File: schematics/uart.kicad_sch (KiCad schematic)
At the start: 5 parts, among them U10 W65C51NxP, Y2 1.8432MHz

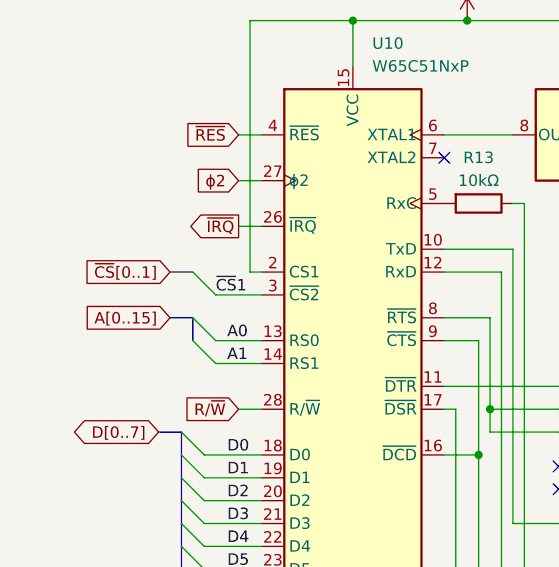
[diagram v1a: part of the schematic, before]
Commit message: Address decoder pld file and no-VIA keyboard schematic and pld file.
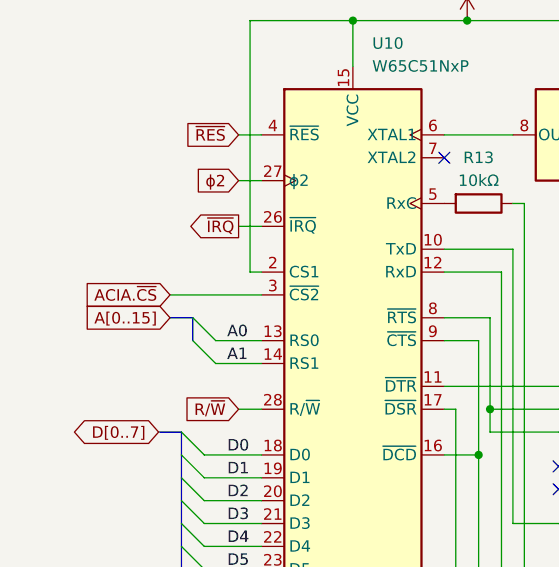
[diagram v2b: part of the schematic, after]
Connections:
- net ~{CS}1 renamed ACIA.~{CS}

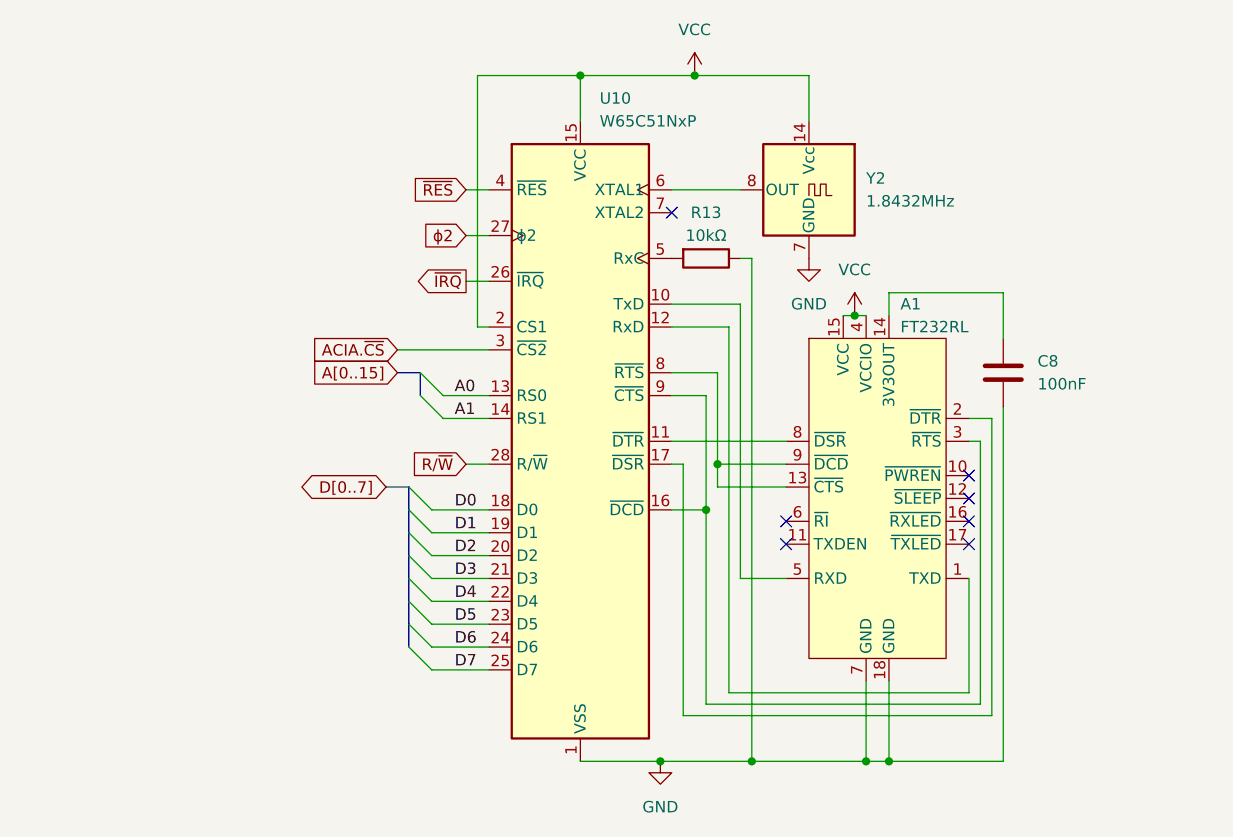
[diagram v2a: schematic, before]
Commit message: PLD files and schematics for address decoder, device selector, keyboard controller, lcd controller, banked memory, and bootloader.
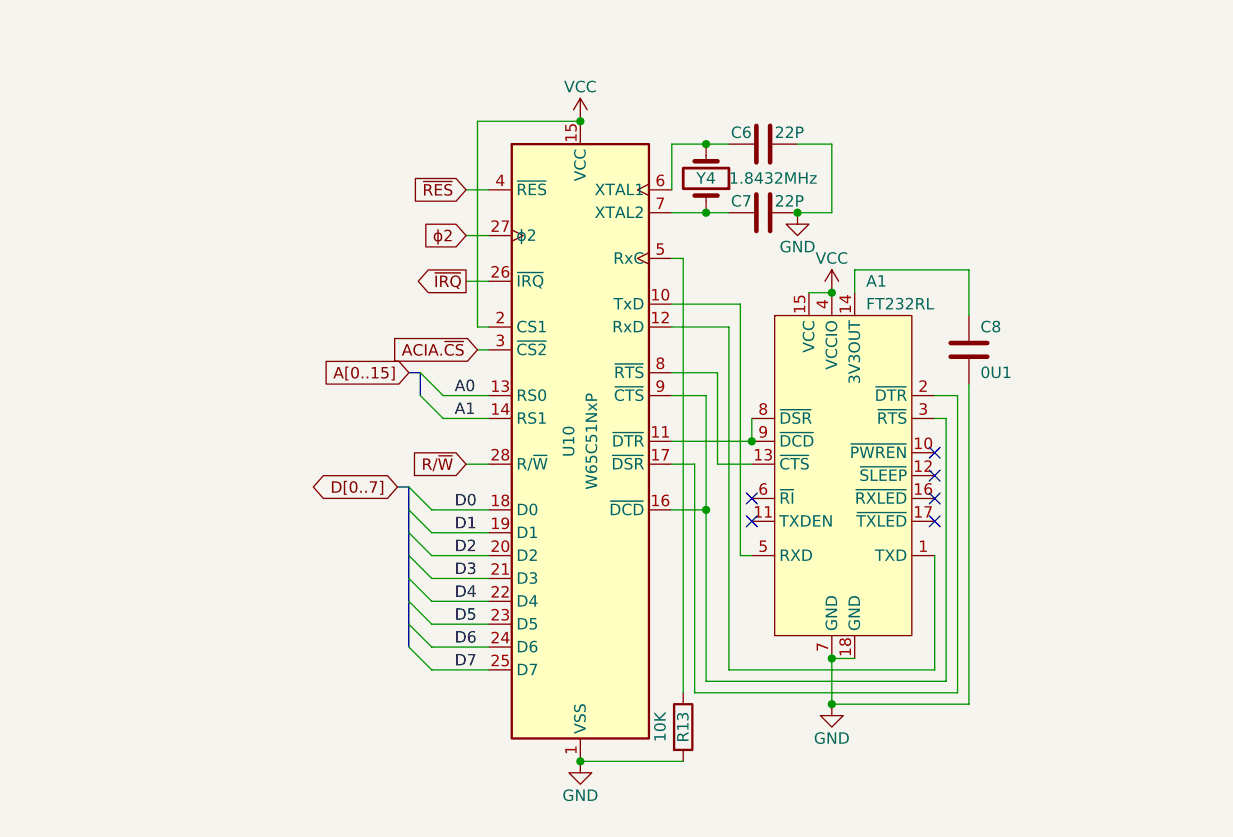
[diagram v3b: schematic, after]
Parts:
- removed Y2: 1.8432MHz, Oscillator:Oscillator_DIP-14, symbol Oscillator:DGOF5S3
- added C6, C7: 22P, symbol Device:C
- added Y4: 1.8432MHz, symbol Device:Crystal
- C8: value 100nF -> 0U1
- R13: value 10kΩ -> 10K
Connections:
- net GND: now also R13.2, C6.2, C7.2; no longer R13.1
- net at A1.8 (~{DSR}), U10.11 (~{DTR}): now also A1.9 (~{DCD})
- net at U10.5 (RxC): now also R13.1; no longer R13.2
- net at U10.6 (XTAL1): now also C6.1, Y4.2
- net at U10.7 (XTAL2): now also C7.1, Y4.1
- net at A1.13 (~{CTS}), U10.8 (~{RTS}): no longer A1.9 (~{DCD})
- no-connect marks 7 -> 6
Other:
- moved on the sheet: A1, C8

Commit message: keyboard, via, acia updates, ready to test
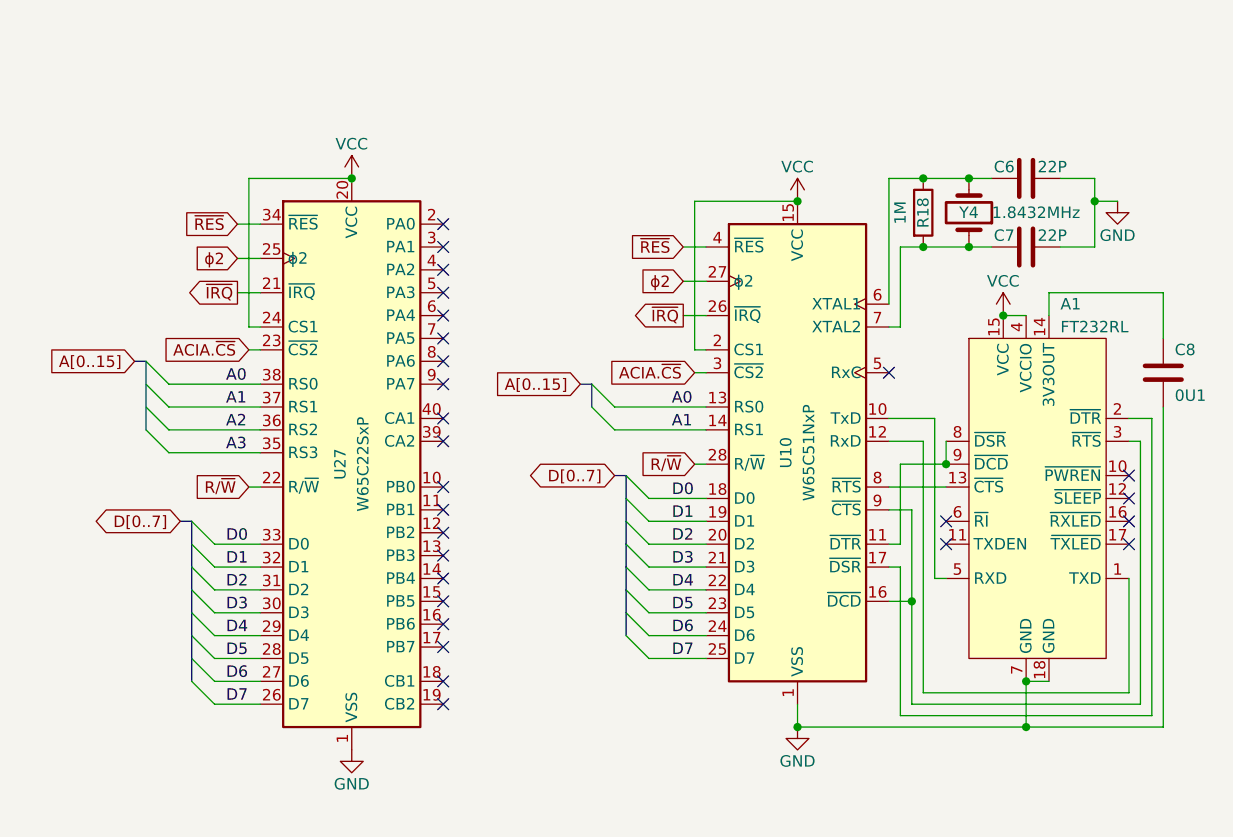
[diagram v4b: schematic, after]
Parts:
- removed R13: 10K, symbol Device:R
- added R18: 1M, symbol Device:R
- added U27: W65C22SxP, Package_DIP:DIP-40_W15.24mm, symbol 65xx-library:W65C22SxP
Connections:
- net A0: now also U27.38 (RS0)
- net A1: now also U27.37 (RS1)
- net ACIA.~{CS}: now also U27.23 (~{CS2})
- net D0: now also U27.33 (D0)
- net D1: now also U27.32 (D1)
- net D2: now also U27.31 (D2)
- net D3: now also U27.30 (D3)
- net D4: now also U27.29 (D4)
- net D5: now also U27.28 (D5)
- net D6: now also U27.27 (D6)
- net D7: now also U27.26 (D7)
- net GND: now also U27.1 (VSS)
- net R/~{W}: now also U27.22 (R/~{W})
- net VCC: now also U27.20 (VCC), U27.24 (CS1)
- net ~{IRQ}: now also U27.21 (~{IRQ})
- net ~{RES}: now also U27.34 (~{RES})
- net ϕ2: now also U27.25 (ϕ2)
- net at C6.1, U10.6 (XTAL1), Y4.2: now also R18.1
- net at C7.1, U10.7 (XTAL2), Y4.1: now also R18.2
- new net A2: U27.36 (RS2)
- new net A3: U27.35 (RS3)
- no-connect marks 6 -> 27
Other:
- moved on the sheet: A1, C8, U10

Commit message: added phi0 for write latch timing
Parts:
- removed C6, C7: 22P, symbol Device:C
- removed R18: 1M, symbol Device:R
- removed U27: W65C22SxP, Package_DIP:DIP-40_W15.24mm, symbol 65xx-library:W65C22SxP
- removed Y4: 1.8432MHz, symbol Device:Crystal
- added Y1: 1.8432MHz, Oscillator:Oscillator_DIP-14, symbol Oscillator:ACO-xxxMHz
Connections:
- net GND: now also Y1.7 (GND)
- net VCC: now also Y1.14 (Vcc)
- net at U10.6 (XTAL1): now also Y1.8 (OUT)
- no-connect marks 27 -> 8

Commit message: updating schematics as I wire the board
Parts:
- renumbered U10 to U15, Y1 to Y2
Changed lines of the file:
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@@
 		(in_pos_files yes)
 		(dnp no)
-		(property "Reference" "U10"
+		(property "Reference" "U15"
 			(at 152.4 99.06 90)
 			(show_name no)
@@
 			(project "bv6502_hw"
 				(path "/94c72abe-aaa5-49aa-8ab7-5d3e7cbc10be/79decbb9-0443-4d8e-a639-28f3b5de1557"
-					(reference "U10")
+					(reference "U15")
 					(unit 1)
 				)
@@
 		(in_pos_files yes)
 		(dnp no)
-		(property "Reference" "#PWR042"
+		(property "Reference" "#PWR034"
 			(at 171.45 87.63 0)
 			(hide yes)
@@
 			(project "bv6502_hw"
 				(path "/94c72abe-aaa5-49aa-8ab7-5d3e7cbc10be/79decbb9-0443-4d8e-a639-28f3b5de1557"
-					(reference "#PWR042")
+					(reference "#PWR034")
 					(unit 1)
 				)
@@
 		(in_pos_files yes)
 		(dnp no)
-		(property "Reference" "Y1"
+		(property "Reference" "Y2"
 			(at 172.72 64.77 0)
 			(show_name no)
@@
 			(project "bv6502_hw"
 				(path "/94c72abe-aaa5-49aa-8ab7-5d3e7cbc10be/79decbb9-0443-4d8e-a639-28f3b5de1557"
-					(reference "Y1")
+					(reference "Y2")
 					(unit 1)
 				)
@@
 		(in_pos_files yes)
 		(dnp no)
-		(property "Reference" "#PWR024"
+		(property "Reference" "#PWR033"
 			(at 171.45 69.85 0)
 			(hide yes)
@@
 			(project "bv6502_hw"
 				(path "/94c72abe-aaa5-49aa-8ab7-5d3e7cbc10be/79decbb9-0443-4d8e-a639-28f3b5de1557"
-					(reference "#PWR024")
+					(reference "#PWR033")
 					(unit 1)
 				)
@@
 		(in_pos_files yes)
 		(dnp no)
-		(property "Reference" "#PWR022"
+		(property "Reference" "#PWR032"
 			(at 153.67 135.89 0)
 			(hide yes)
@@
 			(project "bv6502_hw"
 				(path "/94c72abe-aaa5-49aa-8ab7-5d3e7cbc10be/79decbb9-0443-4d8e-a639-28f3b5de1557"
-					(reference "#PWR022")
+					(reference "#PWR032")
 					(unit 1)
 				)
@@
 		(in_pos_files yes)
 		(dnp no)
-		(property "Reference" "#PWR025"
+		(property "Reference" "#PWR035"
 			(at 176.53 87.63 0)
 			(hide yes)
@@
 			(project "bv6502_hw"
 				(path "/94c72abe-aaa5-49aa-8ab7-5d3e7cbc10be/79decbb9-0443-4d8e-a639-28f3b5de1557"
-					(reference "#PWR025")
+					(reference "#PWR035")
 					(unit 1)
 				)
@@
 		(in_pos_files yes)
 		(dnp no)
-		(property "Reference" "#PWR023"
+		(property "Reference" "#PWR031"
 			(at 153.67 74.93 0)
 			(hide yes)
@@
 			(project "bv6502_hw"
 				(path "/94c72abe-aaa5-49aa-8ab7-5d3e7cbc10be/79decbb9-0443-4d8e-a639-28f3b5de1557"
-					(reference "#PWR023")
-					(unit 1)
-				)
+					(reference "#PWR031")
+					(unit 1)
+				)

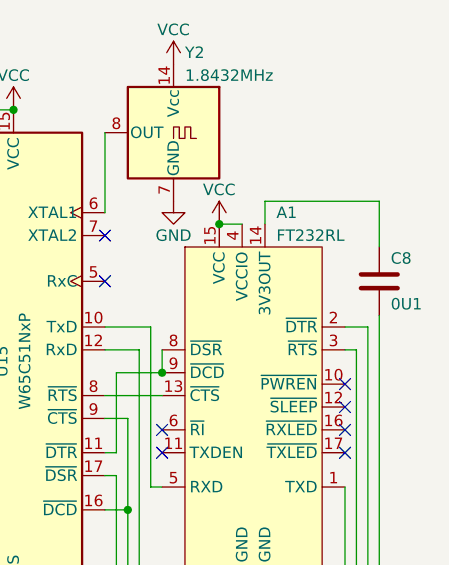
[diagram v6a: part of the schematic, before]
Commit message: my keyboard needed a transceiver after all :(
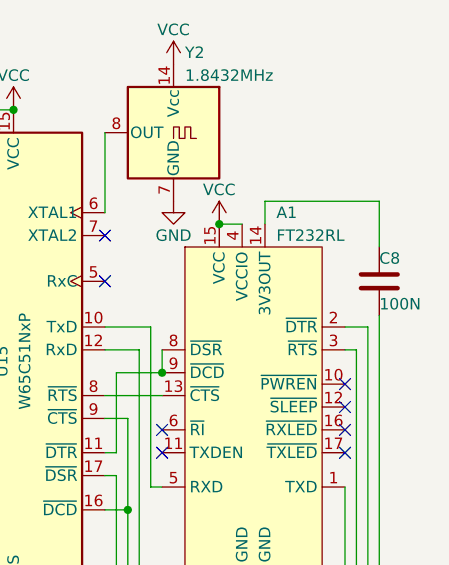
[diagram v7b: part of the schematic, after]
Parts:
- C8: value 0U1 -> 100N
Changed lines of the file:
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@@
 		(dnp no)
 		(property "Reference" "C8"
-			(at 195.58 87.63 0)
+			(at 194.31 87.63 0)
 			(show_name no)
 			(do_not_autoplace no)
@@
 			)
 		)
-		(property "Value" "0U1"
-			(at 195.58 92.71 0)
+		(property "Value" "100N"
+			(at 194.31 92.71 0)
 			(show_name no)
 			(do_not_autoplace no)
